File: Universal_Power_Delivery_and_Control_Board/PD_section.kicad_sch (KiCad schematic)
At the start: 46 parts, among them Q2 AO3401A, U1 TPS259470LRPWR, U2 CH224Q_C46061833, U3 USBLC6-2SC6, U4 ESD2CAN24-ES, U5 S2B-ZR (LF)(SN), U6 USBLC6-2SC6, U7 TPS54202DDC

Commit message: Added some misc stuff layout almost finished.
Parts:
- removed C12: 47uF, lcsc_footprints:C77101_C1210, symbol lcsc_imported:GRM32ER61C476KE15L
- removed F1: 06H1100D, lcsc_footprints:C182303_F0603, symbol lcsc_imported:06H1100D
- removed Q2: AO3401A, lcsc_footprints:C15127_SOT-23_L2_9-W1_3-P1_90-LS2_4-BR, symbol lcsc_imported:AO3401A
- added C1: 1uF, Capacitor_SMD:C_0603_1608Metric_Pad1.08x0.95mm_HandSolder, symbol Device:C
- added C26: 47uF, lcsc_footprints:C426659_C1206, symbol lcsc_imported:GRM31CR61A476KE15L
- added C44: 10nF, Capacitor_SMD:C_0402_1005Metric_Pad0.74x0.62mm_HandSolder, symbol Device:C
- added F1: Fuse, Fuse:Fuse_1206_3216Metric_Pad1.42x1.75mm_HandSolder, symbol Device:Fuse
- added JP10, JP7, JP8, JP9: SolderJumper_2_Open, Jumper:SolderJumper-2_P1.3mm_Open_RoundedPad1.0x1.5mm, symbol Jumper:SolderJumper_2_Open
- added R22: ?, Resistor_SMD:R_0402_1005Metric_Pad0.72x0.64mm_HandSolder, symbol Device:R
- added R23, R24: 1K, Resistor_SMD:R_0402_1005Metric_Pad0.72x0.64mm_HandSolder, symbol Device:R
- added U18: LM66200DRLR, lcsc_footprints:C3235556_SOT-583-8_L2_1-W1_2-P0_50-LS1_6-BL, symbol lcsc_imported:LM66200DRLR
- added U21: TPS22919DCK, Package_TO_SOT_SMD:SOT-363_SC-70-6, symbol Power_Management:TPS22919DCK
- R11, R15: value 13.3K -> ?
- R3, R6: value 1K -> 4.7K
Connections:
- net +12V_PD: now also C10.2, C11.2, C9.1, U7.3 (VIN), JP10.1 (A), JP9.1 (A)
- net +5V_VSYS: now also JP7.1 (A), JP8.1 (A), U18.2 (VOUT), U18.7 (VOUT)
- net GND: now also C1.2, C26.1, C44.2, R23.1, U18.1 (GND), U18.5 (GND), U21.2 (GND)
- net TPS54202_OUTPUT: now also C26.2, U18.6 (VIN2)
- net at R15.2: now also R22.1
- net at USBC2.A4B9 (VBUS), USBC2.B4A9 (VBUS): now also U6.5 (VBUS), C1.1, F1.2, R24.1, U21.1 (IN)
- net +5V_VBUS renamed VBUS
- net VBUS: now also F1.1, JP10.2 (B), JP7.2 (B), JP8.2 (B), JP9.2 (B), U18.3 (VIN1), U21.5 (QOD), U21.6 (OUT); no longer U6.5 (VBUS)
- new net: C44.1, R24.2, U21.3 (ON)
- new net: R23.2, U18.4 (ON#)
- new net ST_ID: U18.8 (ST)
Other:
- moved on the sheet: R15, TP4, TP5

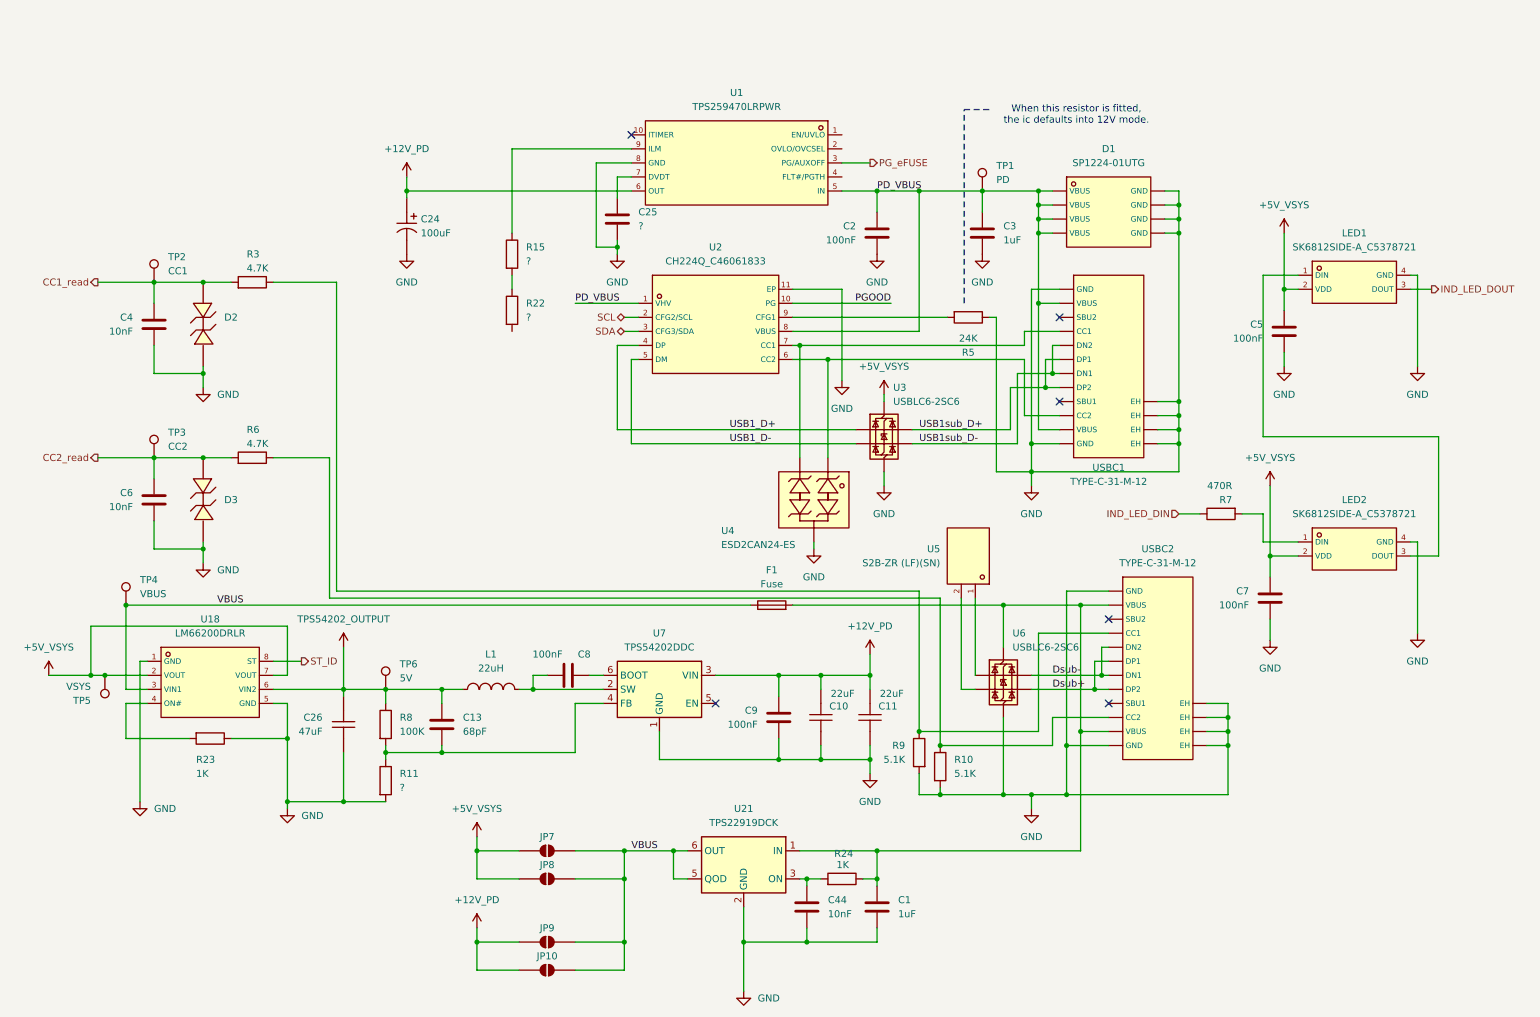
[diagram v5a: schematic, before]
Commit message: Practically finished layout, need to route the buttons.
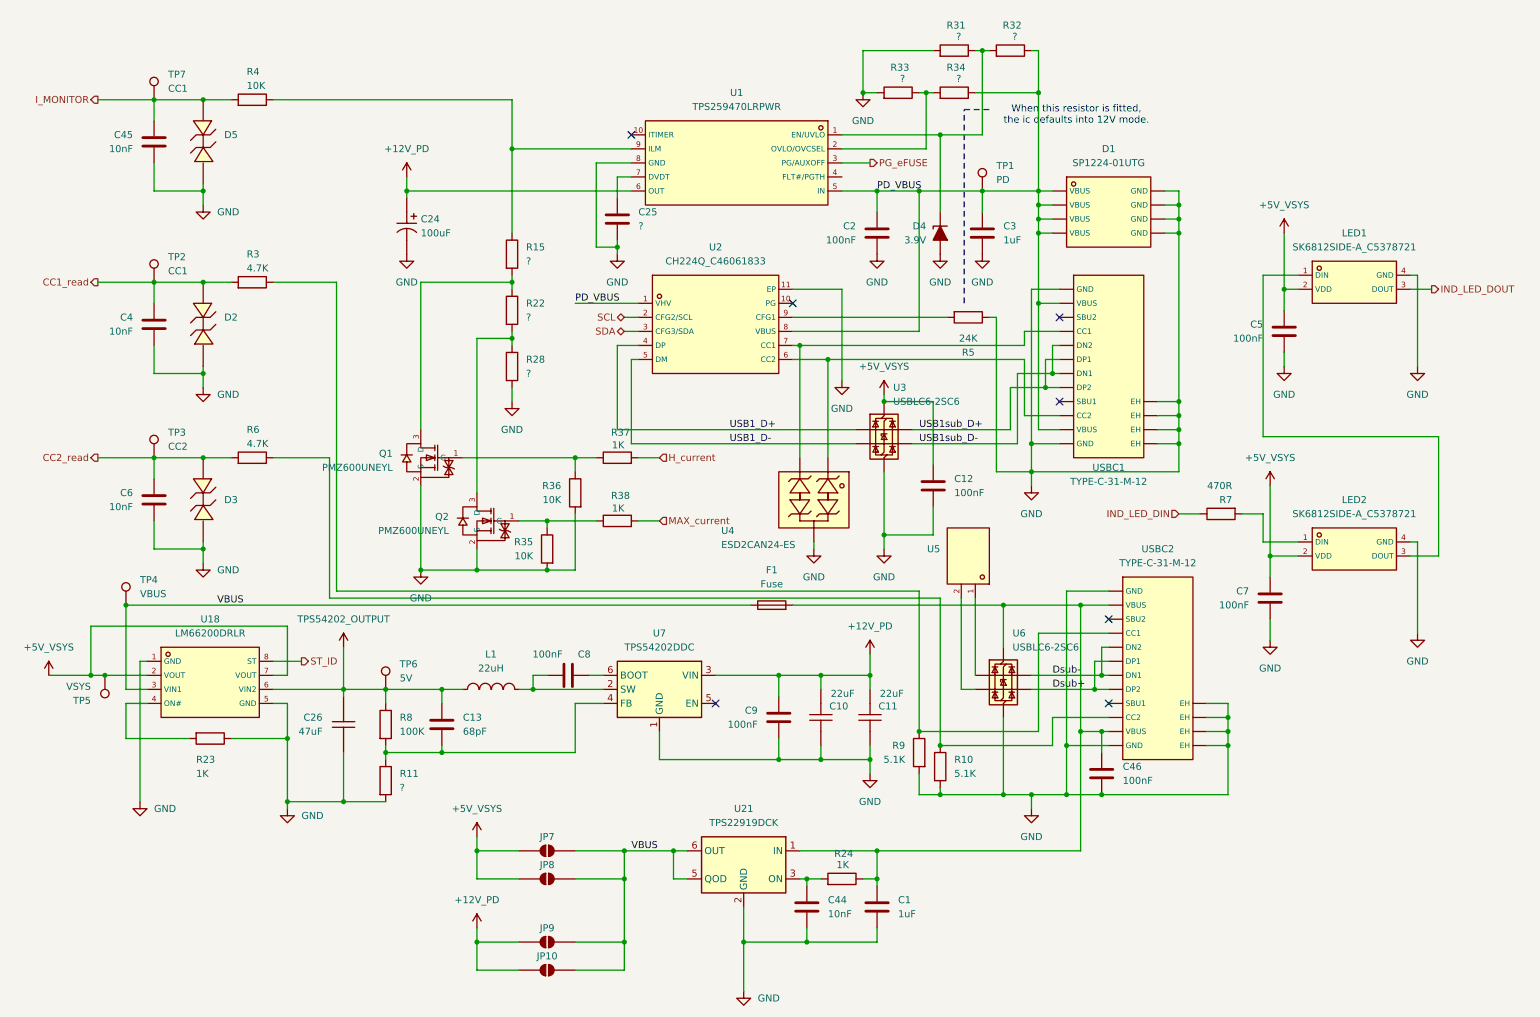
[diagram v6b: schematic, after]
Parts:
- added C12, C46: 100nF, Capacitor_SMD:C_0402_1005Metric_Pad0.74x0.62mm_HandSolder, symbol Device:C
- added C45: 10nF, Capacitor_SMD:C_0402_1005Metric_Pad0.74x0.62mm_HandSolder, symbol Device:C
- added D4: 3.9V, Diode_SMD:D_SOD-882, symbol Device:D_Zener_Filled
- added D5: PESDNC2FD3V3BS, lcsc_footprints:C496536_DFN1006-2L-BI, symbol lcsc_imported:PESDNC2FD3V3BS
- added Q1, Q2: PMZ600UNEYL, lcsc_footprints:C547286_SOT-883-3_L1_0-W0_6-BR, symbol lcsc_imported:PMZ600UNEYL
- added R28: ?, Resistor_SMD:R_0402_1005Metric, symbol Device:R
- added R31, R32, R33, R34: ?, Resistor_SMD:R_0402_1005Metric_Pad0.72x0.64mm_HandSolder, symbol Device:R
- added R35, R36: 10K, Resistor_SMD:R_0402_1005Metric, symbol Device:R
- added R37, R38: 1K, Resistor_SMD:R_0402_1005Metric_Pad0.72x0.64mm_HandSolder, symbol Device:R
- added R4: 10K, Resistor_SMD:R_0402_1005Metric_Pad0.72x0.64mm_HandSolder, symbol Device:R
- added TP7: CC1, TestPoint:TestPoint_Pad_D1.0mm, symbol Connector:TestPoint
- C25: footprint Capacitor_SMD:C_0402_1005Metric_Pad0.74x0.62mm_HandSolder -> Capacitor_SMD:C_0402_1005Metric
- C3: footprint Capacitor_SMD:C_0805_2012Metric_Pad1.18x1.45mm_HandSolder -> Capacitor_SMD:C_0805_2012Metric
- R15, R22: footprint Resistor_SMD:R_0402_1005Metric_Pad0.72x0.64mm_HandSolder -> Resistor_SMD:R_0402_1005Metric
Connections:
- net +5V_VSYS: now also C12.1
- net GND: now also C12.2, C45.2, C46.2, D4.2 (A), D5.1, Q1.2 (S), Q2.2 (S), R28.2, R31.2, R33.2, R35.2, R36.2
- net PD_VBUS: now also R32.1, R34.1
- net at C1.1, F1.2, R24.1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: now also C46.1
- net at R15.2, R22.1: now also Q1.3 (D)
- net at R22.2: now also Q2.3 (D), R28.1
- net at U1.1 (EN/UVLO): now also D4.1 (K), R31.1, R32.2
- net at U1.2 (OVLO/OVCSEL): now also R33.1, R34.2
- net at R15.1, U1.9 (ILM): now also R4.1
- net PGOOD: no longer names the net of U2.10 (PG)
- new net: Q2.1 (G), R35.1, R38.1
- new net: Q1.1 (G), R36.1, R37.1
- new net H_current: R37.2
- new net I_MONITOR: C45.1, D5.2, R4.2, TP7.1
- new net MAX_current: R38.2
- no-connect marks 6 -> 7

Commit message: Fished layout for now, need to add some components for optional functionality.
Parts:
- removed C5, C7: 100nF, Capacitor_SMD:C_0402_1005Metric_Pad0.74x0.62mm_HandSolder, symbol Device:C
- removed LED1, LED2: SK6812SIDE-A_C5378721, lcsc_footprints:C5378721_LED-SMD_4P-L4_0-W1_6-L, symbol lcsc_imported:SK6812SIDE-A_C5378721
- removed R7: 470R, Resistor_SMD:R_0402_1005Metric_Pad0.72x0.64mm_HandSolder, symbol Device:R
- added R46: 10K, Resistor_SMD:R_0402_1005Metric_Pad0.72x0.64mm_HandSolder, symbol Device:R
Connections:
- net PG_eFUSE: now also R46.2
- new net +3V3: R46.1
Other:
- moved on the sheet: C1, C10, C11, C12, C13, C2, C24, C25, C26, C3, C4, C44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

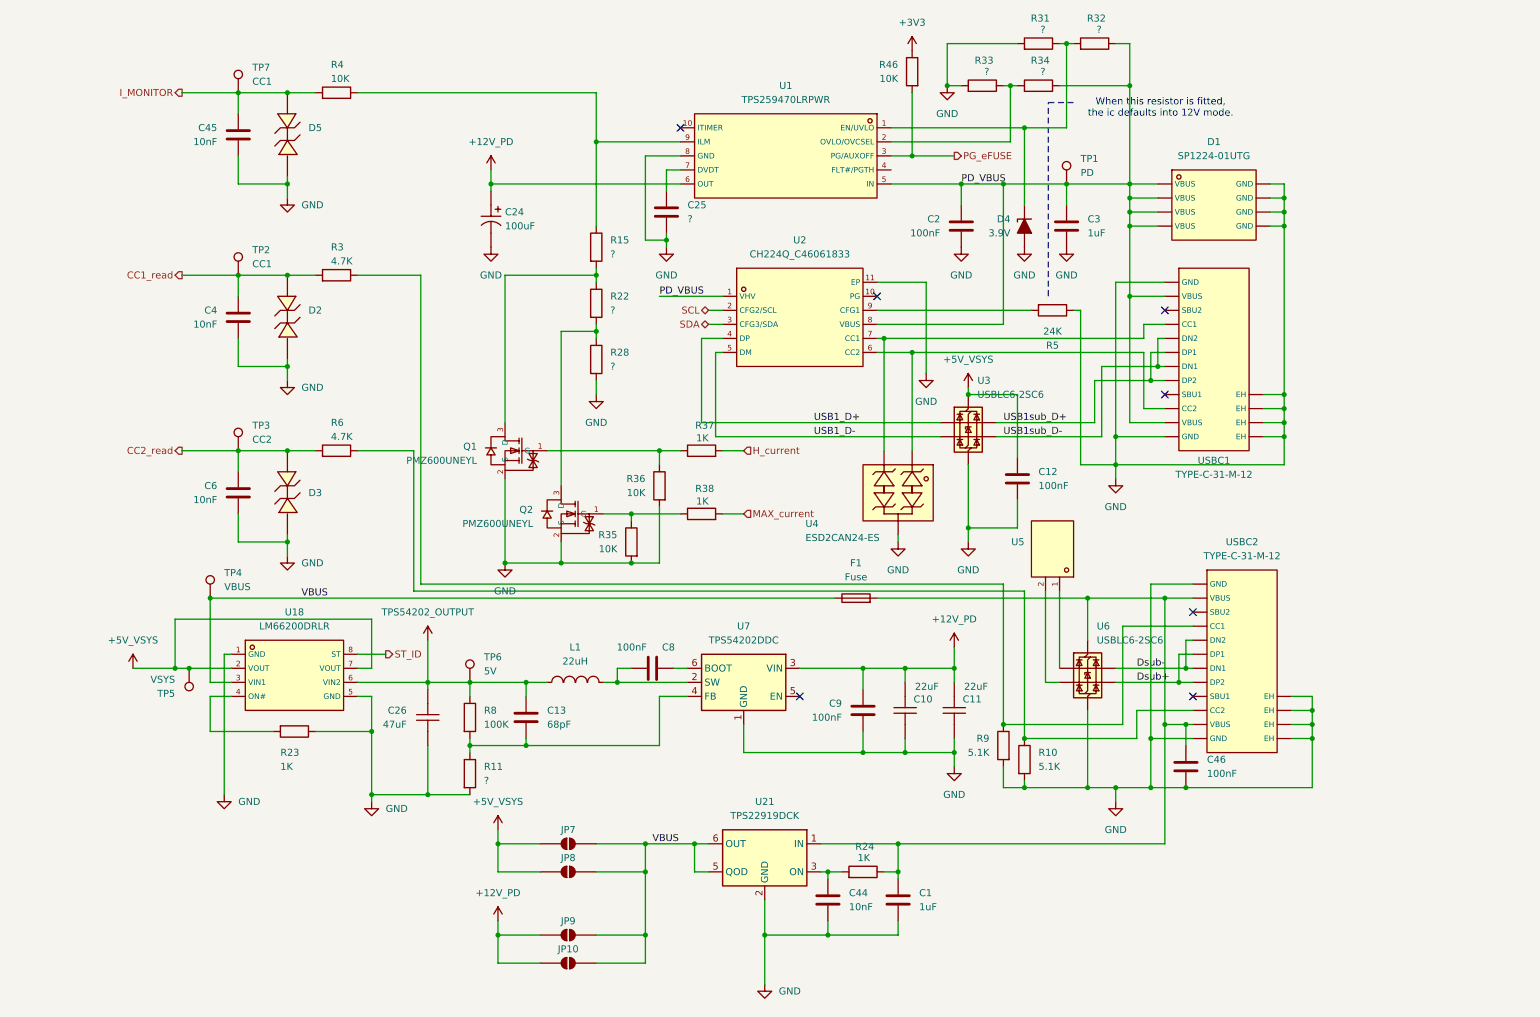
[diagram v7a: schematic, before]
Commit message: Finished layout 0 DRC errors.
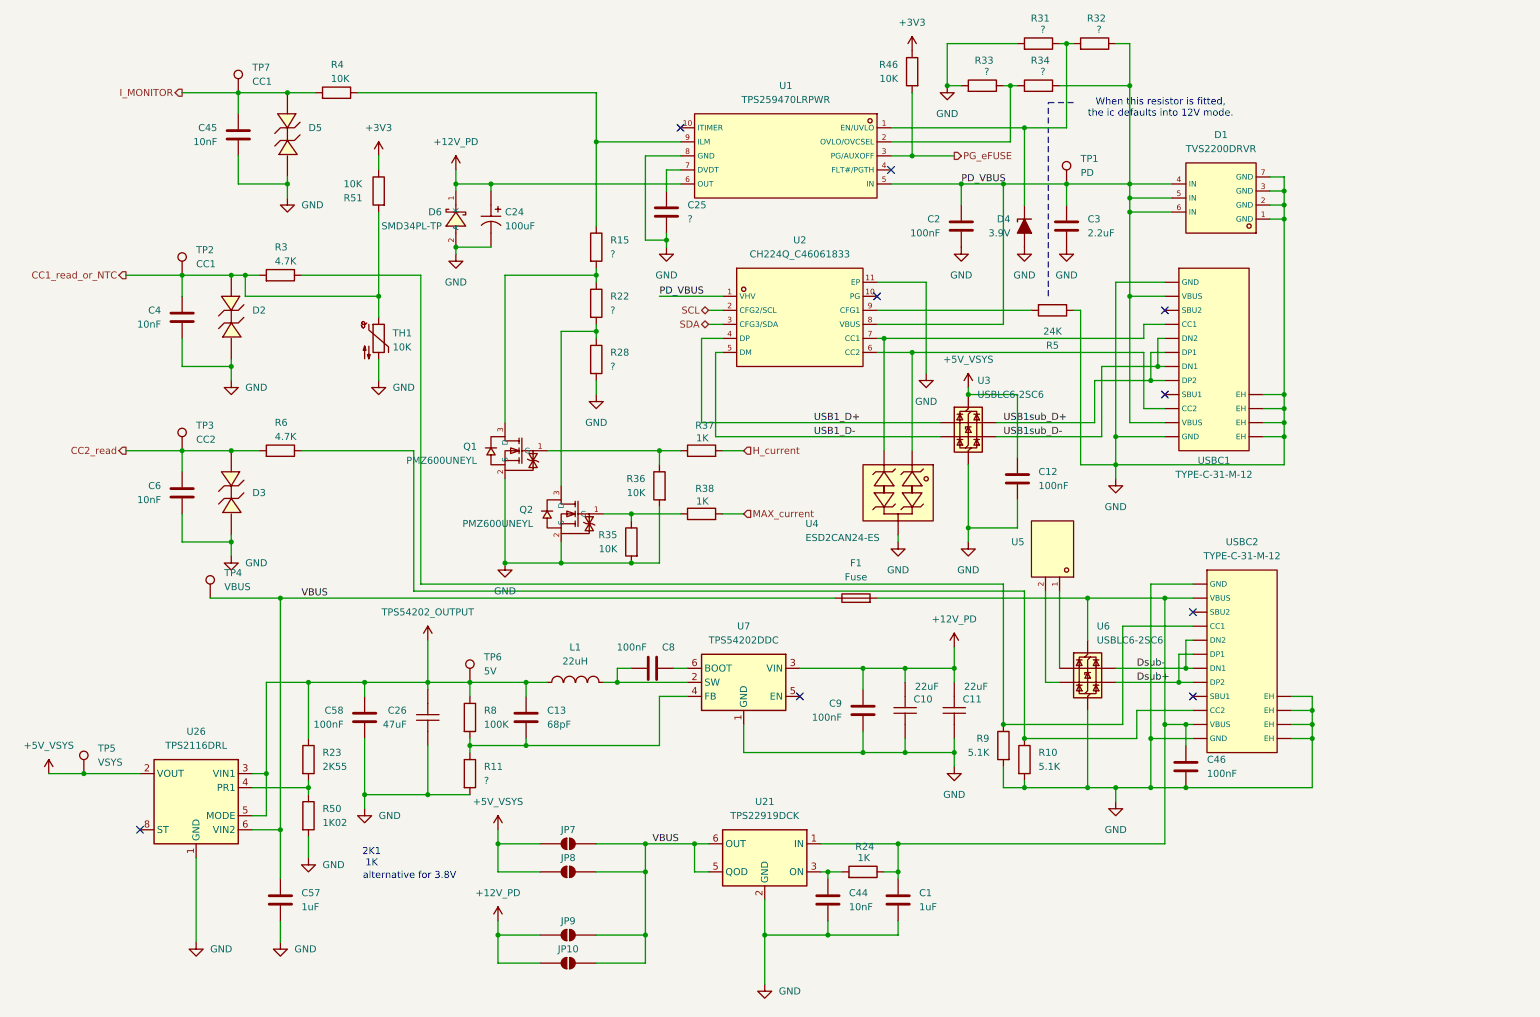
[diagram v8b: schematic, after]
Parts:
- removed D1: SP1224-01UTG, lcsc_footprints:C3705881_DFN-2018-6A_L2_0-W1_8-P0_40-BL-EP, symbol lcsc_imported:SP1224-01UTG
- removed U18: LM66200DRLR, lcsc_footprints:C3235556_SOT-583-8_L2_1-W1_2-P0_50-LS1_6-BL, symbol lcsc_imported:LM66200DRLR
- added C57: 1uF, Capacitor_SMD:C_0402_1005Metric_Pad0.74x0.62mm_HandSolder, symbol Device:C
- added C58: 100nF, Capacitor_SMD:C_0402_1005Metric_Pad0.74x0.62mm_HandSolder, symbol Device:C
- added D1: TVS2200DRVR, lcsc_footprints:C523793_WSON-6_L2_0-W2_0-P0_65-BL-EP, symbol lcsc_imported:TVS2200DRVR
- added D6: SMD34PL-TP, lcsc_footprints:C725481_SOD-123FL_L2_8-W1_7-LS3_6-RD, symbol lcsc_imported:SMD34PL-TP
- added R50: 1K02, Resistor_SMD:R_0402_1005Metric_Pad0.72x0.64mm_HandSolder, symbol Device:R
- added R51: 10K, Resistor_SMD:R_0402_1005Metric_Pad0.72x0.64mm_HandSolder, symbol Device:R
- added TH1: 10K, Resistor_SMD:R_0402_1005Metric_Pad0.72x0.64mm_HandSolder, symbol Device:Thermistor_NTC
- added U26: TPS2116DRL, Package_TO_SOT_SMD:SOT-583-8, symbol Power_Management:TPS2116DRL
- C3: value 1uF -> 2.2uF
- R23: value 1K -> 2K55
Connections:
- net +12V_PD: now also D6.1 (K)
- net +3V3: now also R51.1
- net +5V_VSYS: now also U26.2 (VOUT), U26.7 (VOUT)
- net GND: now also C57.2, C58.2, D1.1 (GND), D1.2 (GND), D1.3 (GND), D1.7 (GND), D6.2 (A), R50.2, TH1.2, U26.1 (GND); no longer R23.1
- net PD_VBUS: now also D1.4 (IN), D1.5 (IN), D1.6 (IN)
- net TPS54202_OUTPUT: now also R23.1, C58.1, U26.3 (VIN1), U26.5 (MODE)
- net VBUS: now also C57.1, U26.6 (VIN2)
- net at R23.2: now also R50.1, U26.4 (PR1)
- net CC1_read renamed CC1_read_or_NTC
- net CC1_read_or_NTC: now also R51.2, TH1.1
- no-connect marks 7 -> 9
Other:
- note added: "2K1 1K"
- note added: "alternative for 3.8V"
- moved on the sheet: C4, C6, D2, D3, R3, R6, TP2, TP3, TP5
